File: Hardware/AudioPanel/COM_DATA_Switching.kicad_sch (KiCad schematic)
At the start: 22 parts, among them J27 Debug Header, SW15 ~{RESET}, SW16 ~{RESET}, SW9 ~{RESET}, U104 MCP23017_ML, U42 ATtiny3227-M, U45 MCP23017_ML, U96 MCP23017_ML, Y7 20MHz

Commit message: Cleaned up stuff, defined more busses
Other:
- sheet 4x4 Crosspoint Switch ports: added VSS; removed none
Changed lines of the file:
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@@
 	(bus
 		(pts
-			(xy 109.22 207.01) (xy 132.08 207.01)
+			(xy 109.22 200.66) (xy 132.08 200.66)
 		)
 		(stroke
@@
 	(bus
 		(pts
-			(xy 132.08 207.01) (xy 132.08 209.55)
+			(xy 132.08 200.66) (xy 132.08 207.01)
 		)
 		(stroke
@@
 		)
 	)
+	(bus
+		(pts
+			(xy 132.08 207.01) (xy 132.08 209.55)
+		)
+		(stroke
+			(width 0)
+			(type default)
+		)
+	)
 	(wire
 		(pts
@@
 		)
 		(pin "{4x4_CROSS}" input
-			(at 109.22 207.01 0)
+			(at 109.22 200.66 0)
+			(effects
+				(font
+					(size 1.27 1.27)
+				)
+				(justify right)
+			)
+		)
+		(pin "VSS" input
+			(at 105.41 191.77 90)
 			(effects
 				(font

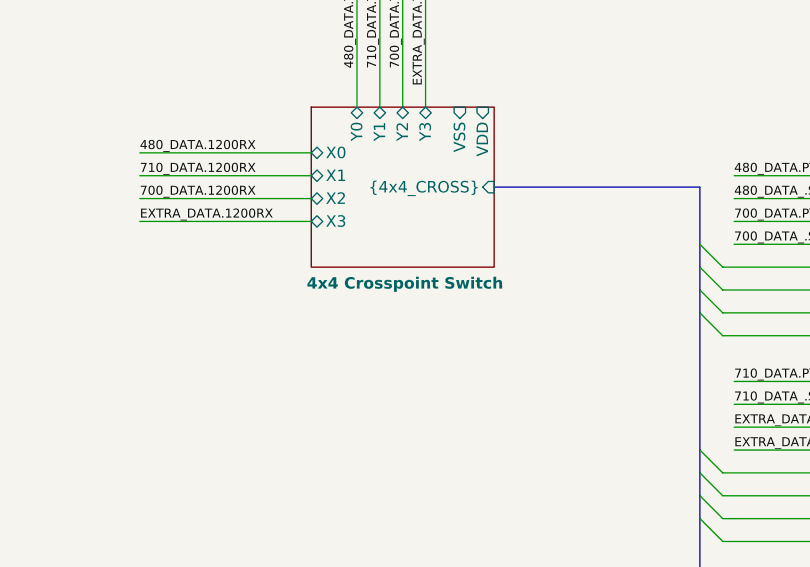
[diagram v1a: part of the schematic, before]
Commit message: Added audio sum amplifiers
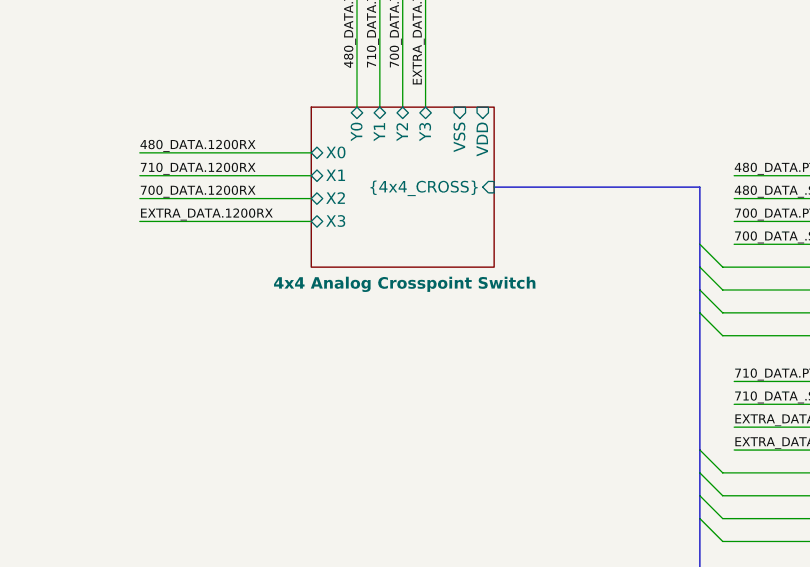
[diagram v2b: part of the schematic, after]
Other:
- sheet 4x4 Crosspoint Switch renamed 4x4 Analog Crosspoint Switch
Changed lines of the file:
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@@
 			(color 128 255 128 1.0000)
 		)
-		(property "Sheetname" "4x4 Crosspoint Switch"
+		(property "Sheetname" "4x4 Analog Crosspoint Switch"
 			(at 99.314 212.09 0)
 			(effects
